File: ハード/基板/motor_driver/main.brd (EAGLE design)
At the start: 35 x 52 mm, 11 parts, among them IC1 TB6643KQ,8

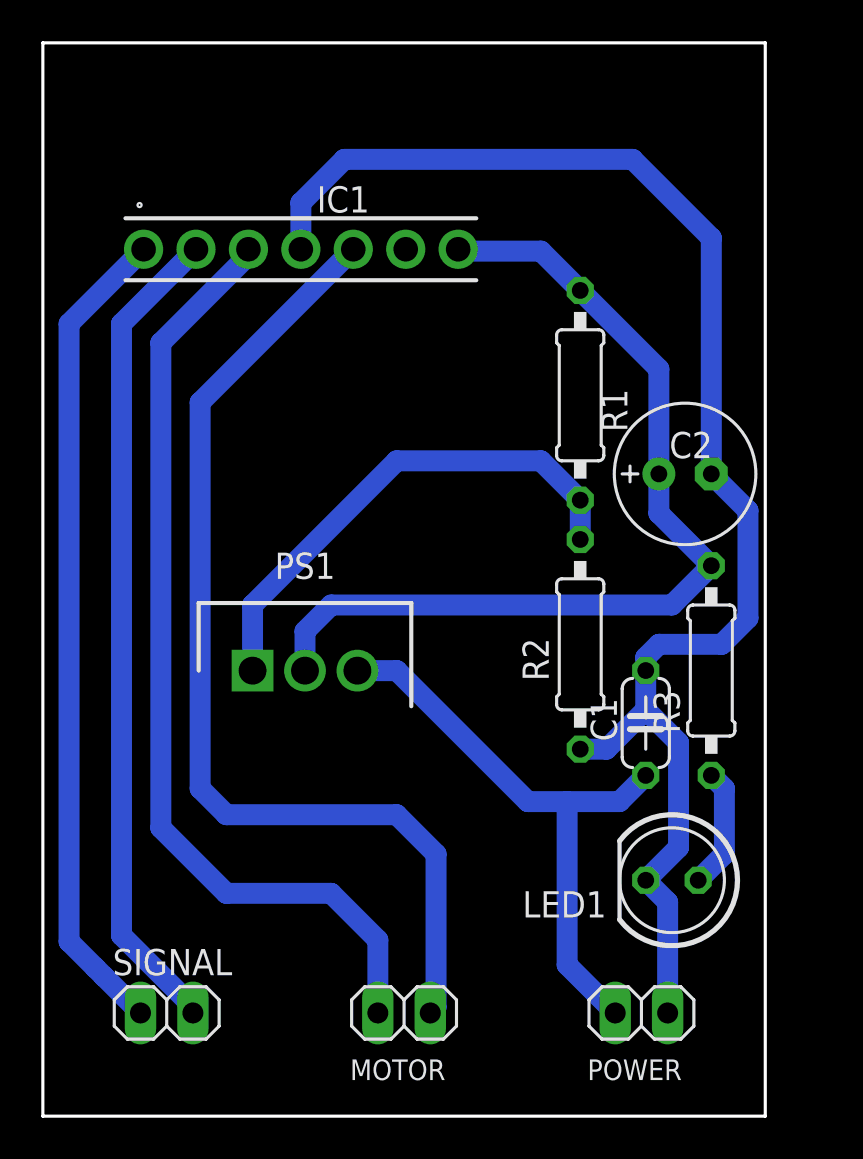
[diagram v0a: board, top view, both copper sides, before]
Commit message: 文字を追加し、デザインを調整
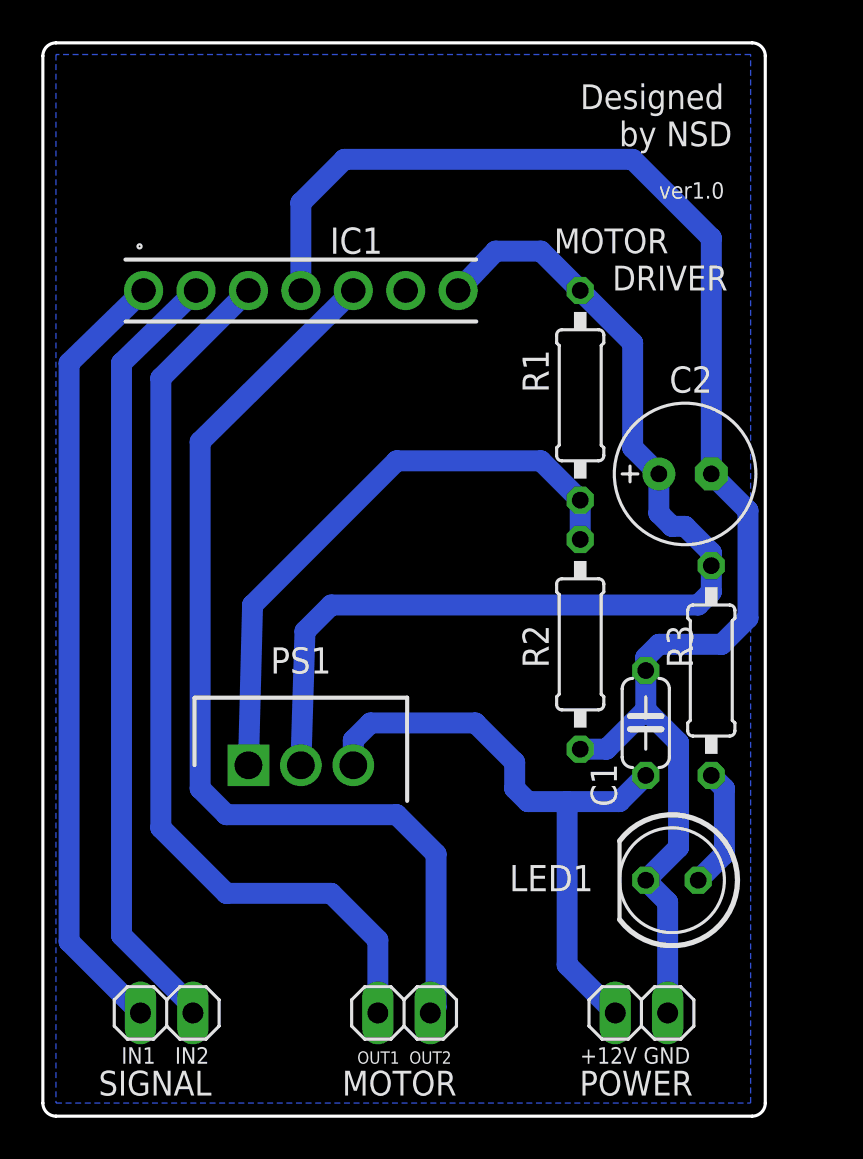
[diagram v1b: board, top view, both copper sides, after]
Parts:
- moved PS1 4.59 mm to (9.96, 17.0)
- moved IC1 2.00 mm to (12.5, 40.0)
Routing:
- net V+: track 45.6 -> 52.1 mm
- net N$3: track 24.6 -> 29.2 mm
- net N$1: track 46.1 -> 44.1 mm
- net GND: track 72.4 -> 74.4 mm
- net N$2: track 49.8 -> 47.8 mm
- net N$5: track 39.9 -> 38.0 mm
- net N$4: track 40.1 -> 38.1 mm
- net +12V: track 28.3 -> 29.8 mm
- added copper zone on layer 16, net N$7
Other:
- outline, holes or cut-outs redrawn
- board text added: "+12V GND"
- board text added: "Designed by NSD"
- board text added: "IN1 IN2"
- board text added: "MOTOR DRIVER"
- board text added: "OUT1 OUT2"
- board text added: "ver1.0"
